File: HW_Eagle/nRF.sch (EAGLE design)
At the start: 6 parts, among them X1 B4B-ZR, X4 22-23-2041, X5 22-23-2041

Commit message: Add regulator
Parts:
- added C1, C2: (no value), rcl:C-USC0805
- added P1: (no value), Voltage Regulator:XC6206SOT-89
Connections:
- new net V_BAT: C2.1, JP2.1, P1.IN
- net GND: now also C1.2, C2.2, P1.VSS
- net MPU6050_SCL: now also X4-1.S; no longer X4-2.S
- net MPU6050_SDA: now also X4-2.S; no longer X4-1.S
- net VCC: now also C1.1, P1.OUT; no longer JP2.1
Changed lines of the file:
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@@
 <part name="JP2" library="pinhead" library_urn="urn:adsk.eagle:library:325" deviceset="PINHD-1X1" device="" package3d_urn="urn:adsk.eagle:package:22485/2"/>
 <part name="GND3" library="supply1" deviceset="GND" device=""/>
-<part name="P+4" library="supply1" deviceset="VCC" device=""/>
 <part name="X4" library="con-molex" library_urn="urn:adsk.eagle:library:165" deviceset="22-23-2041" device=""/>
 <part name="X5" library="con-molex" library_urn="urn:adsk.eagle:library:165" deviceset="22-23-2041" device=""/>
+<part name="C1" library="rcl" library_urn="urn:adsk.eagle:library:334" deviceset="C-US" device="C0805" package3d_urn="urn:adsk.eagle:package:23617/2"/>
+<part name="C2" library="rcl" library_urn="urn:adsk.eagle:library:334" deviceset="C-US" device="C0805" package3d_urn="urn:adsk.eagle:package:23617/2"/>
+<part name="P+5" library="supply1" deviceset="VCC" device=""/>
+<part name="GND5" library="supply1" deviceset="GND" device=""/>
+<part name="GND6" library="supply1" deviceset="GND" device=""/>
+<part name="GND8" library="supply1" deviceset="GND" device=""/>
+<part name="P1" library="Voltage Regulator" deviceset="XC6206" device="SOT-89"/>
 </parts>
 <sheets>
@@
 <instance part="JP2" gate="G$1" x="-71.12" y="86.36" rot="R180"/>
 <instance part="GND3" gate="1" x="-50.8" y="91.44" rot="R90"/>
-<instance part="P+4" gate="VCC" x="-50.8" y="86.36" rot="R270"/>
 <instance part="X4" gate="-1" x="-96.52" y="119.38" rot="R180"/>
 <instance part="X4" gate="-2" x="-96.52" y="121.92" rot="R180"/>
@@
 <instance part="X5" gate="-3" x="-96.52" y="106.68" rot="R180"/>
 <instance part="X5" gate="-4" x="-96.52" y="109.22" rot="R180"/>
+<instance part="C1" gate="G$1" x="-55.88" y="63.5"/>
+<instance part="C2" gate="G$1" x="-99.06" y="48.26"/>
+<instance part="P+5" gate="VCC" x="-55.88" y="78.74"/>
+<instance part="GND5" gate="1" x="-99.06" y="38.1"/>
+<instance part="GND6" gate="1" x="-55.88" y="55.88"/>
+<instance part="GND8" gate="1" x="-83.82" y="40.64"/>
+<instance part="P1" gate="G$1" x="-83.82" y="63.5"/>
 </instances>
 <busses>
@@
 <pinref part="GND3" gate="1" pin="GND"/>
 </segment>
+<segment>
+<pinref part="C2" gate="G$1" pin="2"/>
+<pinref part="GND5" gate="1" pin="GND"/>
+<wire x1="-99.06" y1="40.64" x2="-99.06" y2="43.18" width="0.1524" layer="91"/>
+</segment>
+<segment>
+<pinref part="C1" gate="G$1" pin="2"/>
+<pinref part="GND6" gate="1" pin="GND"/>
+</segment>
+<segment>
+<pinref part="P1" gate="G$1" pin="VSS"/>
+<pinref part="GND8" gate="1" pin="GND"/>
+<wire x1="-83.82" y1="43.18" x2="-83.82" y2="55.88" width="0.1524" layer="91"/>
+</segment>
 </net>
 <net name="VCC" class="0">
@@
 </segment>
 <segment>
-<pinref part="JP2" gate="G$1" pin="1"/>
-<wire x1="-68.58" y1="86.36" x2="-53.34" y2="86.36" width="0.1524" layer="91"/>
-<pinref part="P+4" gate="VCC" pin="VCC"/>
+<pinref part="C1" gate="G$1" pin="1"/>
+<pinref part="P+5" gate="VCC" pin="VCC"/>
+<wire x1="-55.88" y1="76.2" x2="-55.88" y2="71.12" width="0.1524" layer="91"/>
+<wire x1="-55.88" y1="71.12" x2="-55.88" y2="66.04" width="0.1524" layer="91"/>
+<wire x1="-71.12" y1="71.12" x2="-55.88" y2="71.12" width="0.1524" layer="91"/>
+<wire x1="-71.12" y1="71.12" x2="-71.12" y2="66.04" width="0.1524" layer="91"/>
+<pinref part="P1" gate="G$1" pin="OUT"/>
+<wire x1="-71.12" y1="66.04" x2="-73.66" y2="66.04" width="0.1524" layer="91"/>
 </segment>
 </net>
@@
 <net name="MPU6050_SCL" class="0">
 <segment>
-<wire x1="-93.98" y1="121.92" x2="-68.58" y2="121.92" width="0.1524" layer="91"/>
-<label x="-68.58" y="121.92" size="1.778" layer="95"/>
-<pinref part="X4" gate="-2" pin="S"/>
-</segment>
-<segment>
 <pinref part="U4" gate="G$1" pin="P0.04"/>
 <wire x1="12.7" y1="30.48" x2="12.7" y2="50.8" width="0.1524" layer="91"/>
+<label x="12.7" y="30.48" size="1.778" layer="95" rot="R90"/>
+</segment>
+<segment>
+<pinref part="X4" gate="-1" pin="S"/>
+<wire x1="-93.98" y1="119.38" x2="-71.12" y2="119.38" width="0.1524" layer="91"/>
+<label x="-91.44" y="119.38" size="1.778" layer="95"/>
 </segment>
 </net>
@@
 <net name="MPU6050_SDA" class="0">
 <segment>
-<wire x1="-93.98" y1="119.38" x2="-68.58" y2="119.38" width="0.1524" layer="91"/>
-<label x="-83.82" y="119.38" size="1.778" layer="95"/>
-<pinref part="X4" gate="-1" pin="S"/>
-</segment>
-<segment>
 <pinref part="U4" gate="G$1" pin="P0.07"/>
 <wire x1="20.32" y1="50.8" x2="20.32" y2="25.4" width="0.1524" layer="91"/>
+<label x="20.32" y="27.94" size="1.778" layer="95" rot="R90"/>
+</segment>
+<segment>
+<pinref part="X4" gate="-2" pin="S"/>
+<wire x1="-93.98" y1="121.92" x2="-71.12" y2="121.92" width="0.1524" layer="91"/>
+<label x="-91.44" y="121.92" size="1.778" layer="95"/>
 </segment>
 </net>
@@
 <pinref part="U4" gate="G$1" pin="P0.22"/>
 <wire x1="-15.24" y1="88.9" x2="-38.1" y2="88.9" width="0.1524" layer="91"/>
+</segment>
+</net>
+<net name="V_BAT" class="0">
+<segment>
+<pinref part="C2" gate="G$1" pin="1"/>
+<wire x1="-93.98" y1="66.04" x2="-99.06" y2="66.04" width="0.1524" layer="91"/>
+<wire x1="-99.06" y1="66.04" x2="-99.06" y2="50.8" width="0.1524" layer="91"/>
+<pinref part="P1" gate="G$1" pin="IN"/>
+</segment>
+<segment>
+<pinref part="JP2" gate="G$1" pin="1"/>
+<wire x1="-68.58" y1="86.36" x2="-53.34" y2="86.36" width="0.1524" layer="91"/>
 </segment>
 </net>
@@
 packages will not be understood (or retained) with this version.
 </note>
+<note version="8.4" severity="warning">
+Since Version 8.4, EAGLE supports properties for SPICE simulation.
+Probes in schematics and SPICE mapping objects found in parts and library devices
+will not be understood with this version. Update EAGLE to the latest version
+for full support of SPICE simulation.
+</note>
 </compatibility>

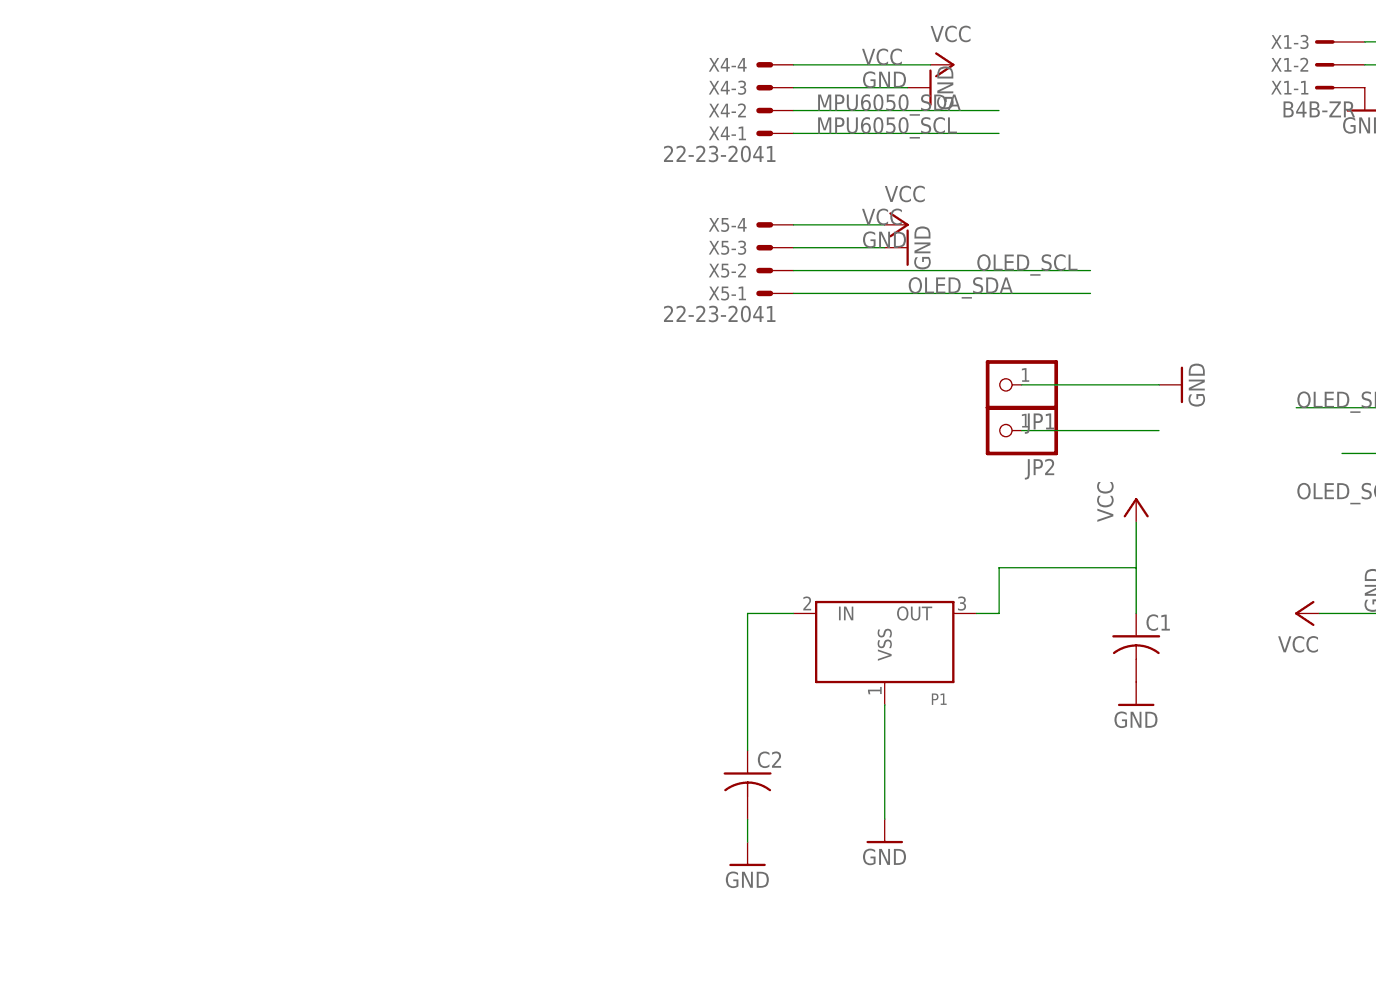
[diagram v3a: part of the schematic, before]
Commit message: [HW] Add modules: Oled, MPU6050, TP4056
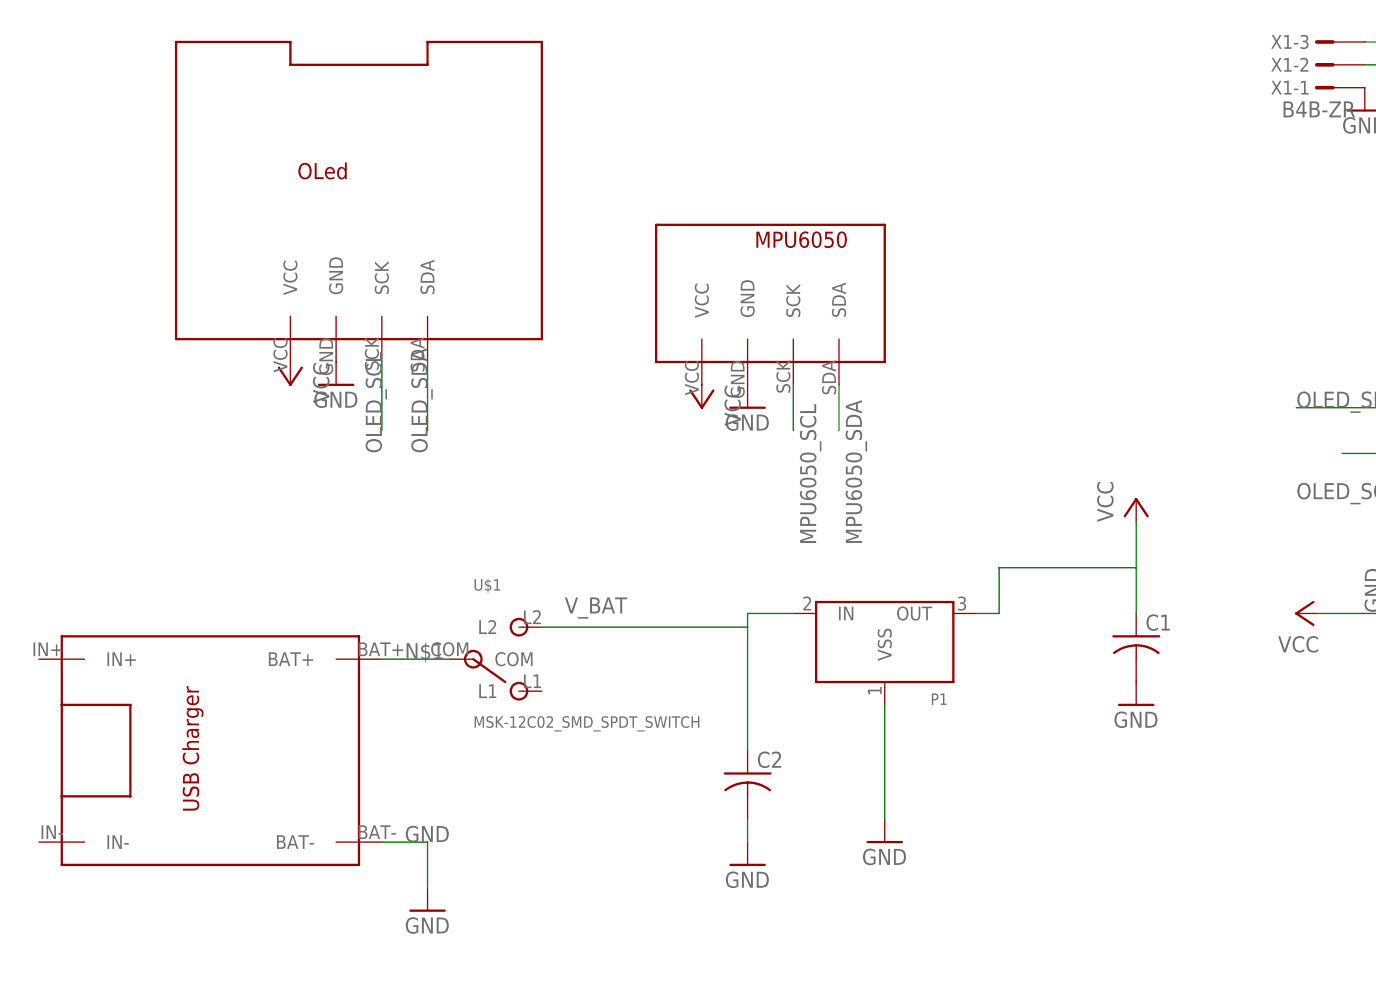
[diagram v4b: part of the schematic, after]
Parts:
- removed JP1, JP2: (no value), pinhead:PINHD-1X1
- removed X4, X5: 22-23-2041, con-molex:22-23-2041
- added U$1: MSK-12C02_SMD_SPDT_SWITCH, MSK-12C02 SMD Micro Slider Switch SPDT 2:MSK-12C02_SMD_SPDT_SWITCH
- added U$2: TP4056, TP4056 charging module:TP4056
- added U$3: OLED, Oled:OLED
- added U$4: MPU60XX, 6050:MPU60XX
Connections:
- new net N$1: U$1.COM, U$2.BAT+
- net GND: now also U$2.BAT-, U$3.GND, U$4.GND; no longer JP1.1, X4-3.S, X5-3.S
- net MPU6050_SCL: now also U$4.SCK; no longer X4-1.S
- net MPU6050_SDA: now also U$4.SDA; no longer X4-2.S
- net OLED_SCL: now also U$3.SCK; no longer X5-2.S
- net OLED_SDA: now also U$3.SDA; no longer X5-1.S
- net VCC: now also U$3.VCC, U$4.VCC; no longer X4-4.S, X5-4.S
- net V_BAT: now also U$1.L2; no longer JP2.1

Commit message: [HW] Update HW v1.2
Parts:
- removed U4: (no value), YJ-14015:YJ-14015
- added C3: (no value), rcl:C-USC0603
- added R1: (no value), rcl:R-US_R0603
- added TS-3625-W: MOMENTARY-SWITCH-SPST-SMD-6.0X3.5MM, SparkFun-Switches:MOMENTARY-SWITCH-SPST-SMD-6.0X3.5MM
- added U$5: NRF51822, nrf51822:NRF51822
- renumbered U$2 to U$6
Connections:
- new net BUTTON: C3.1, R1.1, TS-3625-W.2, U$5.P04
- net GND: now also C3.2, TS-3625-W.1, U$5.GND; no longer U4.GND@1, U4.GND@2
- net MPU6050_SCL: now also U$5.P08; no longer U4.P0.04
- net MPU6050_SDA: now also U$5.P06; no longer U4.P0.07
- net OLED_SCL: now also U$5.P30; no longer U4.P0.24
- net OLED_SDA: now also U$5.P01; no longer U4.P0.22
- net SWDCLK: now also U$5.SWDCLK; no longer U4.SWDCLK
- net SWDIO: now also U$5.SWDIO; no longer U4.SWDIO/NRESET
- net VCC: now also R1.2, U$5.VCC; no longer U4.VDD
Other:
- moved on the sheet: C1, X1-1, X1-2, X1-3
